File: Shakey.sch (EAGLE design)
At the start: 84 parts, among them CN1 CONN_USB-4UCON-11071, U1 ATMEGA32U4-AU, U2 ICM-20689, U3 AP2210K-3.3TRG1, U4 LM75AD, Y1 16Mhz

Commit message: ready for production
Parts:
- SJ1: value SOLDER JUMPER -> SOLDER_JUMPER
- TP1: value TPB2,54 -> TESTPAD; device testpad:TPB2,54 -> SixthLogic:TESTPAD-2.54MM
- renumbered U$7 to JP2, U$8 to JP1
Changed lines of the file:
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@@
 <grid distance="0.1" unitdist="inch" unit="inch" style="lines" multiple="1" display="no" altdistance="0.01" altunitdist="inch" altunit="inch"/>
 <layers>
-<layer number="1" name="Top" color="4" fill="1" visible="yes" active="no"/>
-<layer number="2" name="Route2" color="1" fill="3" visible="yes" active="no"/>
-<layer number="3" name="Route3" color="4" fill="3" visible="yes" active="no"/>
-<layer number="4" name="Route4" color="1" fill="4" visible="yes" active="no"/>
-<layer number="5" name="Route5" color="4" fill="4" visible="yes" active="no"/>
-<layer number="6" name="Route6" color="1" fill="8" visible="yes" active="no"/>
-<layer number="7" name="Route7" color="4" fill="8" visible="yes" active="no"/>
-<layer number="8" name="Route8" color="1" fill="2" visible="yes" active="no"/>
-<layer number="9" name="Route9" color="4" fill="2" visible="yes" active="no"/>
-<layer number="10" name="Route10" color="1" fill="7" visible="yes" active="no"/>
-<layer number="11" name="Route11" color="4" fill="7" visible="yes" active="no"/>
-<layer number="12" name="Route12" color="1" fill="5" visible="yes" active="no"/>
-<layer number="13" name="Route13" color="4" fill="5" visible="yes" active="no"/>
-<layer number="14" name="Route14" color="1" fill="6" visible="yes" active="no"/>
-<layer number="15" name="Route15" color="4" fill="6" visible="yes" active="no"/>
-<layer number="16" name="Bottom" color="1" fill="1" visible="yes" active="no"/>
-<layer number="17" name="Pads" color="2" fill="1" visible="yes" active="no"/>
-<layer number="18" name="Vias" color="2" fill="1" visible="yes" active="no"/>
-<layer number="19" name="Unrouted" color="6" fill="1" visible="yes" active="no"/>
-<layer number="20" name="Dimension" color="15" fill="1" visible="yes" active="no"/>
-<layer number="21" name="tPlace" color="7" fill="1" visible="yes" active="no"/>
-<layer number="22" name="bPlace" color="7" fill="1" visible="yes" active="no"/>
-<layer number="23" name="tOrigins" color="15" fill="1" visible="yes" active="no"/>
-<layer number="24" name="bOrigins" color="15" fill="1" visible="yes" active="no"/>
-<layer number="25" name="tNames" color="7" fill="1" visible="yes" active="no"/>
-<layer number="26" name="bNames" color="7" fill="1" visible="yes" active="no"/>
-<layer number="27" name="tValues" color="7" fill="1" visible="yes" active="no"/>
-<layer number="28" name="bValues" color="7" fill="1" visible="yes" active="no"/>
+<layer number="1" name="Top" color="4" fill="1" visible="no" active="no"/>
+<layer number="2" name="Route2" color="1" fill="3" visible="no" active="no"/>
+<layer number="3" name="Route3" color="4" fill="3" visible="no" active="no"/>
+<layer number="4" name="Route4" color="1" fill="4" visible="no" active="no"/>
+<layer number="5" name="Route5" color="4" fill="4" visible="no" active="no"/>
+<layer number="6" name="Route6" color="1" fill="8" visible="no" active="no"/>
+<layer number="7" name="Route7" color="4" fill="8" visible="no" active="no"/>
+<layer number="8" name="Route8" color="1" fill="2" visible="no" active="no"/>
+<layer number="9" name="Route9" color="4" fill="2" visible="no" active="no"/>
+<layer number="10" name="Route10" color="1" fill="7" visible="no" active="no"/>
+<layer number="11" name="Route11" color="4" fill="7" visible="no" active="no"/>
+<layer number="12" name="Route12" color="1" fill="5" visible="no" active="no"/>
+<layer number="13" name="Route13" color="4" fill="5" visible="no" active="no"/>
+<layer number="14" name="Route14" color="1" fill="6" visible="no" active="no"/>
+<layer number="15" name="Route15" color="4" fill="6" visible="no" active="no"/>
+<layer number="16" name="Bottom" color="1" fill="1" visible="no" active="no"/>
+<layer number="17" name="Pads" color="2" fill="1" visible="no" active="no"/>
+<layer number="18" name="Vias" color="2" fill="1" visible="no" active="no"/>
+<layer number="19" name="Unrouted" color="6" fill="1" visible="no" active="no"/>
+<layer number="20" name="Dimension" color="15" fill="1" visible="no" active="no"/>
+<layer number="21" name="tPlace" color="7" fill="1" visible="no" active="no"/>
+<layer number="22" name="bPlace" color="7" fill="1" visible="no" active="no"/>
+<layer number="23" name="tOrigins" color="15" fill="1" visible="no" active="no"/>
+<layer number="24" name="bOrigins" color="15" fill="1" visible="no" active="no"/>
+<layer number="25" name="tNames" color="7" fill="1" visible="no" active="no"/>
+<layer number="26" name="bNames" color="7" fill="1" visible="no" active="no"/>
+<layer number="27" name="tValues" color="7" fill="1" visible="no" active="no"/>
+<layer number="28" name="bValues" color="7" fill="1" visible="no" active="no"/>
 <layer number="29" name="tStop" color="7" fill="3" visible="no" active="no"/>
 <layer number="30" name="bStop" color="7" fill="6" visible="no" active="no"/>
@@
 <layer number="35" name="tGlue" color="7" fill="4" visible="no" active="no"/>
 <layer number="36" name="bGlue" color="7" fill="5" visible="no" active="no"/>
-<layer number="37" name="tTest" color="7" fill="1" visible="yes" active="no"/>
-<layer number="38" name="bTest" color="7" fill="1" visible="yes" active="no"/>
+<layer number="37" name="tTest" color="7" fill="1" visible="no" active="no"/>
+<layer number="38" name="bTest" color="7" fill="1" visible="no" active="no"/>
 <layer number="39" name="tKeepout" color="4" fill="11" visible="no" active="no"/>
 <layer number="40" name="bKeepout" color="1" fill="11" visible="no" active="no"/>
@@
 <layer number="44" name="Drills" color="7" fill="1" visible="no" active="no"/>
 <layer number="45" name="Holes" color="7" fill="1" visible="no" active="no"/>
-<layer number="46" name="Milling" color="3" fill="1" visible="yes" active="no"/>
-<layer number="47" name="Measures" color="7" fill="1" visible="yes" active="no"/>
-<layer number="48" name="Document" color="7" fill="1" visible="yes" active="no"/>
-<layer number="49" name="Reference" color="7" fill="1" visible="yes" active="no"/>
-<layer number="50" name="dxf" color="7" fill="1" visible="yes" active="no"/>
-<layer number="51" name="tDocu" color="6" fill="1" visible="yes" active="no"/>
-<layer number="52" name="bDocu" color="6" fill="1" visible="yes" active="no"/>
-<layer number="53" name="tGND_GNDA" color="7" fill="9" visible="yes" active="no"/>
-<layer number="54" name="bGND_GNDA" color="1" fill="9" visible="yes" active="no"/>
-<layer number="56" name="wert" color="7" fill="1" visible="yes" active="no"/>
-<layer number="57" name="tCAD" color="7" fill="1" visible="yes" active="no"/>
-<layer number="59" name="tCarbon" color="7" fill="1" visible="yes" active="no"/>
-<layer number="60" name="bCarbon" color="7" fill="1" visible="yes" active="no"/>
+<layer number="46" name="Milling" color="3" fill="1" visible="no" active="no"/>
+<layer number="47" name="Measures" color="7" fill="1" visible="no" active="no"/>
+<layer number="48" name="Document" color="7" fill="1" visible="no" active="no"/>
+<layer number="49" name="Reference" color="7" fill="1" visible="no" active="no"/>
+<layer number="50" name="dxf" color="7" fill="1" visible="no" active="no"/>
+<layer number="51" name="tDocu" color="6" fill="1" visible="no" active="no"/>
+<layer number="52" name="bDocu" color="6" fill="1" visible="no" active="no"/>
+<layer number="53" name="tGND_GNDA" color="7" fill="9" visible="no" active="no"/>
+<layer number="54" name="bGND_GNDA" color="1" fill="9" visible="no" active="no"/>
+<layer number="56" name="wert" color="7" fill="1" visible="no" active="no"/>
+<layer number="57" name="tCAD" color="7" fill="1" visible="no" active="no"/>
+<layer number="59" name="tCarbon" color="7" fill="1" visible="no" active="no"/>
+<layer number="60" name="bCarbon" color="7" fill="1" visible="no" active="no"/>
 <layer number="88" name="SimResults" color="9" fill="1" visible="yes" active="yes"/>
 <layer number="89" name="SimProbes" color="9" fill="1" visible="yes" active="yes"/>
@@
 </part>
 <part name="P+7" library="supply1" deviceset="VCC" device=""/>
-<part name="SJ1" library="SixthLogic" deviceset="SOLDER_JUMPER_NC" device="" value="SOLDER JUMPER"/>
+<part name="SJ1" library="SixthLogic" deviceset="SOLDER_JUMPER_NC" device="" value="SOLDER_JUMPER"/>
 <part name="TX_LED" library="SixthLogic" deviceset="LED" device="-1206-LTST-BOTTOM" value="YELLOW">
 <attribute name="DESCRIPTION" value="LED YELLOW CLEAR CHIP SMD"/>
@@
 <part name="SUPPLY18" library="supply2" deviceset="GND" device=""/>
 <part name="U$6" library="SixthLogic" deviceset="3.3V" device=""/>
-<part name="U$7" library="SixthLogic" deviceset="FIDUCIAL" device="-1X3MM"/>
-<part name="U$8" library="SixthLogic" deviceset="FIDUCIAL" device="-1X3MM"/>
+<part name="JP2" library="SixthLogic" deviceset="FIDUCIAL" device="-1X3MM" value="FIDUCIAL-1X3MM"/>
+<part name="JP1" library="SixthLogic" deviceset="FIDUCIAL" device="-1X3MM" value="FIDUCIAL-1X3MM"/>
 <part name="U$10" library="SixthLogic" deviceset="FRAME-A3L-LOC" device=""/>
-<part name="TP1" library="testpad" deviceset="TP" device="B2,54" value="TPB2,54"/>
+<part name="TP1" library="SixthLogic" deviceset="TESTPAD" device="-2.54MM" value="TESTPAD"/>
 </parts>
 <sheets>
@@
 </instance>
 <instance part="U$6" gate="G$1" x="254" y="243.84"/>
-<instance part="U$7" gate="G$1" x="379.73" y="11.43"/>
-<instance part="U$8" gate="G$1" x="374.396" y="11.43"/>
+<instance part="JP2" gate="G$1" x="379.73" y="11.43"/>
+<instance part="JP1" gate="G$1" x="374.396" y="11.43"/>
 <instance part="U$10" gate="G$1" x="0" y="0"/>
 <instance part="TP1" gate="G$1" x="68.58" y="231.14"/>

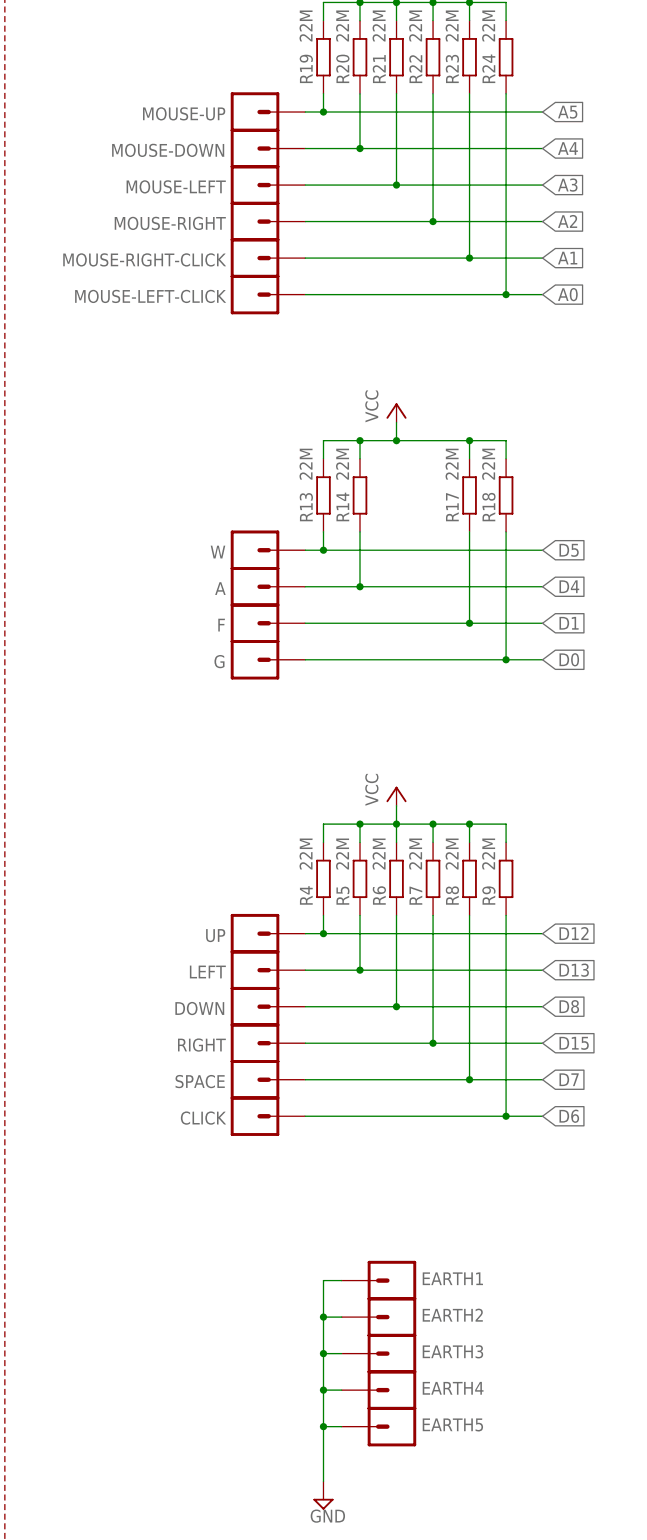
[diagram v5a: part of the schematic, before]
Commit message: changed croc hole to 3.0mm
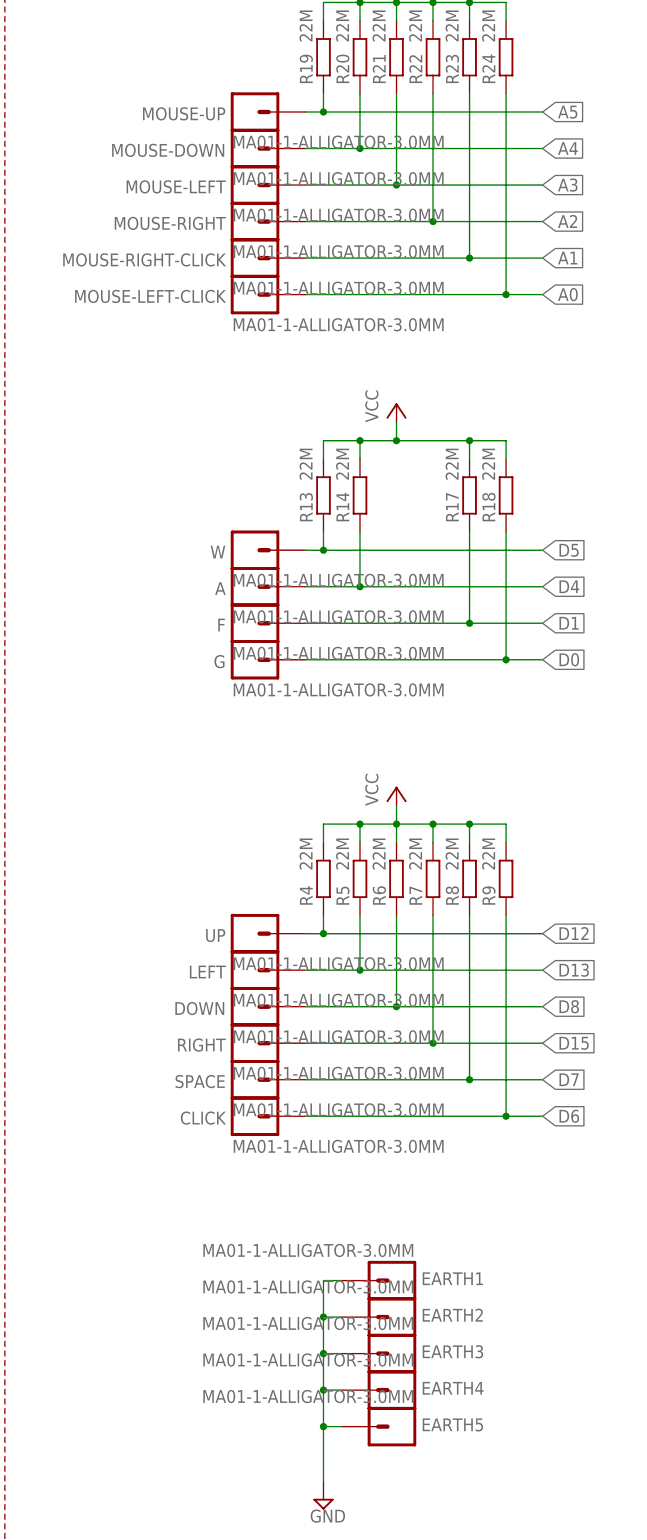
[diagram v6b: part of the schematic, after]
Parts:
- A, CLICK, DOWN, EARTH1, EARTH2, EARTH3, EARTH4, EARTH5, F, G, LEFT, MOUSE-DOWN, MOUSE-LEFT, MOUSE-LEFT-CLICK, MOUSE-RIGHT, MOUSE-RIGHT-CLICK, MOUSE-UP, RIGHT, SPACE, UP, W: value MA01-1-ALLIGATOR-3.1MM -> MA01-1-ALLIGATOR-3.0MM; device SixthLogic:MA01-1-ALLIGATOR-3.1MM -> SixthLogic:MA01-1-ALLIGATOR-3.0MM

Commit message: correct Micro USB value for P&P
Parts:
- CN1: value CONN_USB-4UCON-11071 -> MicroUSB
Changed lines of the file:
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@@
 <grid distance="0.1" unitdist="inch" unit="inch" style="lines" multiple="1" display="no" altdistance="0.01" altunitdist="inch" altunit="inch"/>
 <layers>
-<layer number="1" name="Top" color="4" fill="1" visible="yes" active="no"/>
-<layer number="2" name="Route2" color="1" fill="3" visible="yes" active="no"/>
-<layer number="3" name="Route3" color="4" fill="3" visible="yes" active="no"/>
-<layer number="4" name="Route4" color="1" fill="4" visible="yes" active="no"/>
-<layer number="5" name="Route5" color="4" fill="4" visible="yes" active="no"/>
-<layer number="6" name="Route6" color="1" fill="8" visible="yes" active="no"/>
-<layer number="7" name="Route7" color="4" fill="8" visible="yes" active="no"/>
-<layer number="8" name="Route8" color="1" fill="2" visible="yes" active="no"/>
-<layer number="9" name="Route9" color="4" fill="2" visible="yes" active="no"/>
-<layer number="10" name="Route10" color="1" fill="7" visible="yes" active="no"/>
-<layer number="11" name="Route11" color="4" fill="7" visible="yes" active="no"/>
-<layer number="12" name="Route12" color="1" fill="5" visible="yes" active="no"/>
-<layer number="13" name="Route13" color="4" fill="5" visible="yes" active="no"/>
-<layer number="14" name="Route14" color="1" fill="6" visible="yes" active="no"/>
-<layer number="15" name="Route15" color="4" fill="6" visible="yes" active="no"/>
-<layer number="16" name="Bottom" color="1" fill="1" visible="yes" active="no"/>
-<layer number="17" name="Pads" color="2" fill="1" visible="yes" active="no"/>
-<layer number="18" name="Vias" color="2" fill="1" visible="yes" active="no"/>
-<layer number="19" name="Unrouted" color="6" fill="1" visible="yes" active="no"/>
-<layer number="20" name="Dimension" color="15" fill="1" visible="yes" active="no"/>
-<layer number="21" name="tPlace" color="7" fill="1" visible="yes" active="no"/>
-<layer number="22" name="bPlace" color="7" fill="1" visible="yes" active="no"/>
-<layer number="23" name="tOrigins" color="15" fill="1" visible="yes" active="no"/>
-<layer number="24" name="bOrigins" color="15" fill="1" visible="yes" active="no"/>
-<layer number="25" name="tNames" color="7" fill="1" visible="yes" active="no"/>
-<layer number="26" name="bNames" color="7" fill="1" visible="yes" active="no"/>
-<layer number="27" name="tValues" color="7" fill="1" visible="yes" active="no"/>
-<layer number="28" name="bValues" color="7" fill="1" visible="yes" active="no"/>
+<layer number="1" name="Top" color="4" fill="1" visible="no" active="no"/>
+<layer number="2" name="Route2" color="1" fill="3" visible="no" active="no"/>
+<layer number="3" name="Route3" color="4" fill="3" visible="no" active="no"/>
+<layer number="4" name="Route4" color="1" fill="4" visible="no" active="no"/>
+<layer number="5" name="Route5" color="4" fill="4" visible="no" active="no"/>
+<layer number="6" name="Route6" color="1" fill="8" visible="no" active="no"/>
+<layer number="7" name="Route7" color="4" fill="8" visible="no" active="no"/>
+<layer number="8" name="Route8" color="1" fill="2" visible="no" active="no"/>
+<layer number="9" name="Route9" color="4" fill="2" visible="no" active="no"/>
+<layer number="10" name="Route10" color="1" fill="7" visible="no" active="no"/>
+<layer number="11" name="Route11" color="4" fill="7" visible="no" active="no"/>
+<layer number="12" name="Route12" color="1" fill="5" visible="no" active="no"/>
+<layer number="13" name="Route13" color="4" fill="5" visible="no" active="no"/>
+<layer number="14" name="Route14" color="1" fill="6" visible="no" active="no"/>
+<layer number="15" name="Route15" color="4" fill="6" visible="no" active="no"/>
+<layer number="16" name="Bottom" color="1" fill="1" visible="no" active="no"/>
+<layer number="17" name="Pads" color="2" fill="1" visible="no" active="no"/>
+<layer number="18" name="Vias" color="2" fill="1" visible="no" active="no"/>
+<layer number="19" name="Unrouted" color="6" fill="1" visible="no" active="no"/>
+<layer number="20" name="Dimension" color="15" fill="1" visible="no" active="no"/>
+<layer number="21" name="tPlace" color="7" fill="1" visible="no" active="no"/>
+<layer number="22" name="bPlace" color="7" fill="1" visible="no" active="no"/>
+<layer number="23" name="tOrigins" color="15" fill="1" visible="no" active="no"/>
+<layer number="24" name="bOrigins" color="15" fill="1" visible="no" active="no"/>
+<layer number="25" name="tNames" color="7" fill="1" visible="no" active="no"/>
+<layer number="26" name="bNames" color="7" fill="1" visible="no" active="no"/>
+<layer number="27" name="tValues" color="7" fill="1" visible="no" active="no"/>
+<layer number="28" name="bValues" color="7" fill="1" visible="no" active="no"/>
 <layer number="29" name="tStop" color="7" fill="3" visible="no" active="no"/>
 <layer number="30" name="bStop" color="7" fill="6" visible="no" active="no"/>
@@
 <layer number="35" name="tGlue" color="7" fill="4" visible="no" active="no"/>
 <layer number="36" name="bGlue" color="7" fill="5" visible="no" active="no"/>
-<layer number="37" name="tTest" color="7" fill="1" visible="yes" active="no"/>
-<layer number="38" name="bTest" color="7" fill="1" visible="yes" active="no"/>
+<layer number="37" name="tTest" color="7" fill="1" visible="no" active="no"/>
+<layer number="38" name="bTest" color="7" fill="1" visible="no" active="no"/>
 <layer number="39" name="tKeepout" color="4" fill="11" visible="no" active="no"/>
 <layer number="40" name="bKeepout" color="1" fill="11" visible="no" active="no"/>
@@
 <layer number="44" name="Drills" color="7" fill="1" visible="no" active="no"/>
 <layer number="45" name="Holes" color="7" fill="1" visible="no" active="no"/>
-<layer number="46" name="Milling" color="3" fill="1" visible="yes" active="no"/>
-<layer number="47" name="Measures" color="7" fill="1" visible="yes" active="no"/>
-<layer number="48" name="Document" color="7" fill="1" visible="yes" active="no"/>
-<layer number="49" name="Reference" color="7" fill="1" visible="yes" active="no"/>
-<layer number="50" name="dxf" color="7" fill="1" visible="yes" active="no"/>
-<layer number="51" name="tDocu" color="6" fill="1" visible="yes" active="no"/>
-<layer number="52" name="bDocu" color="6" fill="1" visible="yes" active="no"/>
-<layer number="53" name="tGND_GNDA" color="7" fill="9" visible="yes" active="no"/>
-<layer number="54" name="bGND_GNDA" color="1" fill="9" visible="yes" active="no"/>
-<layer number="56" name="wert" color="7" fill="1" visible="yes" active="no"/>
-<layer number="57" name="tCAD" color="7" fill="1" visible="yes" active="no"/>
-<layer number="59" name="tCarbon" color="7" fill="1" visible="yes" active="no"/>
-<layer number="60" name="bCarbon" color="7" fill="1" visible="yes" active="no"/>
+<layer number="46" name="Milling" color="3" fill="1" visible="no" active="no"/>
+<layer number="47" name="Measures" color="7" fill="1" visible="no" active="no"/>
+<layer number="48" name="Document" color="7" fill="1" visible="no" active="no"/>
+<layer number="49" name="Reference" color="7" fill="1" visible="no" active="no"/>
+<layer number="50" name="dxf" color="7" fill="1" visible="no" active="no"/>
+<layer number="51" name="tDocu" color="6" fill="1" visible="no" active="no"/>
+<layer number="52" name="bDocu" color="6" fill="1" visible="no" active="no"/>
+<layer number="53" name="tGND_GNDA" color="7" fill="9" visible="no" active="no"/>
+<layer number="54" name="bGND_GNDA" color="1" fill="9" visible="no" active="no"/>
+<layer number="56" name="wert" color="7" fill="1" visible="no" active="no"/>
+<layer number="57" name="tCAD" color="7" fill="1" visible="no" active="no"/>
+<layer number="59" name="tCarbon" color="7" fill="1" visible="no" active="no"/>
+<layer number="60" name="bCarbon" color="7" fill="1" visible="no" active="no"/>
 <layer number="88" name="SimResults" color="9" fill="1" visible="yes" active="yes"/>
 <layer number="89" name="SimProbes" color="9" fill="1" visible="yes" active="yes"/>
@@
 </part>
 <part name="P+1" library="supply1" deviceset="VCC" device=""/>
-<part name="CN1" library="SixthLogic" deviceset="CONN_USB" device="-4UCON-11071"/>
+<part name="CN1" library="SixthLogic" deviceset="CONN_USB" device="-4UCON-11071" value="MicroUSB"/>
 <part name="F1" library="SixthLogic" deviceset="PPTC" device="-1206" value="500mA">
 <attribute name="DESCRIPTION" value="PTC RESET FUSE 8V 500MA 1206"/>
